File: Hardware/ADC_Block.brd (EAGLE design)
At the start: 30.5 x 44.5 mm, 28 parts, among them U1 ADS1015, U2 PCA9306

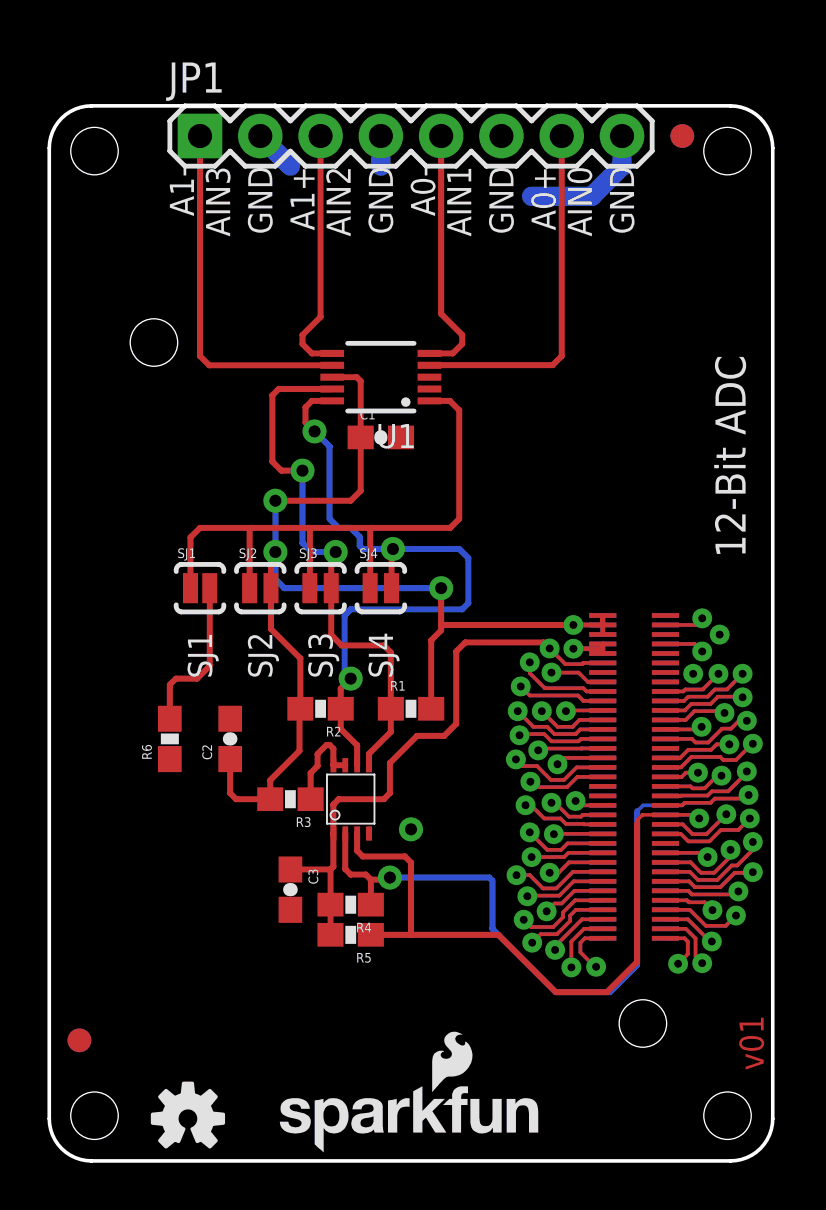
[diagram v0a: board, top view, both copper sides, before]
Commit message: Added DCIN pin Renamed boards and moved name around clenaed up copper pours clenaed up dimensions and units.
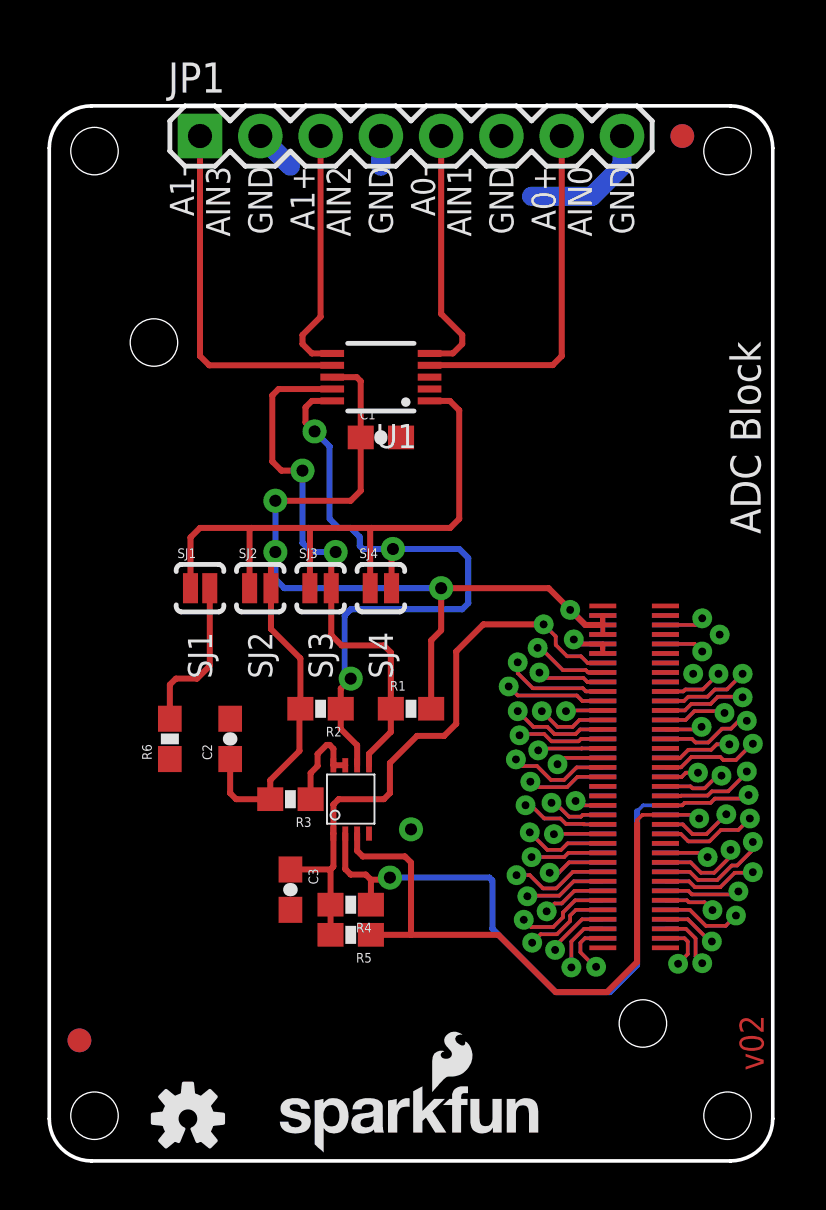
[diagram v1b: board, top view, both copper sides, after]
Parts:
- R4, R5: value 2.2k -> DNP
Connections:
- new net DCIN: U$2.14, U$3.14
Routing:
- net DCIN: track 0.00 -> 6.35 mm, vias 0 -> 1
- net 1.8V: track 26.9 -> 28.5 mm
- net VSYS: track 50.2 -> 51.2 mm
- net USB_DP: track 4.65 -> 5.67 mm
- net USB_DN: track 7.70 -> 8.72 mm
- net USB_VBUS: track 7.42 -> 8.44 mm
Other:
- board text added: "ADC Block"
- board text added: "NOTE: Units are in Inches"
- board text added: "v02"
- board text removed: "12-Bit ADC"
- board text removed: "Connectors Go Here"
- board text removed: "LED's and selector switches go here"
- board text removed: "Max Board Length"
- board text removed: "Nothing goes here... I mean it."
- board text removed: "v01"

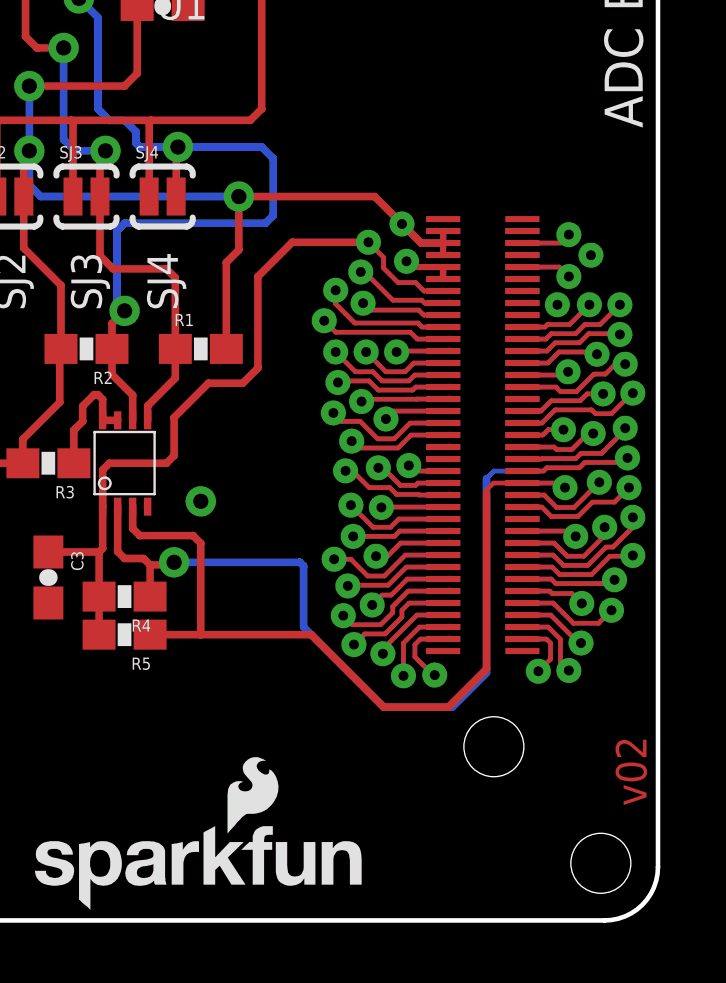
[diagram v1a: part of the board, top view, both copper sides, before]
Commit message: Chg pullups to 10k, update gnd and pwr traces, rev to 10
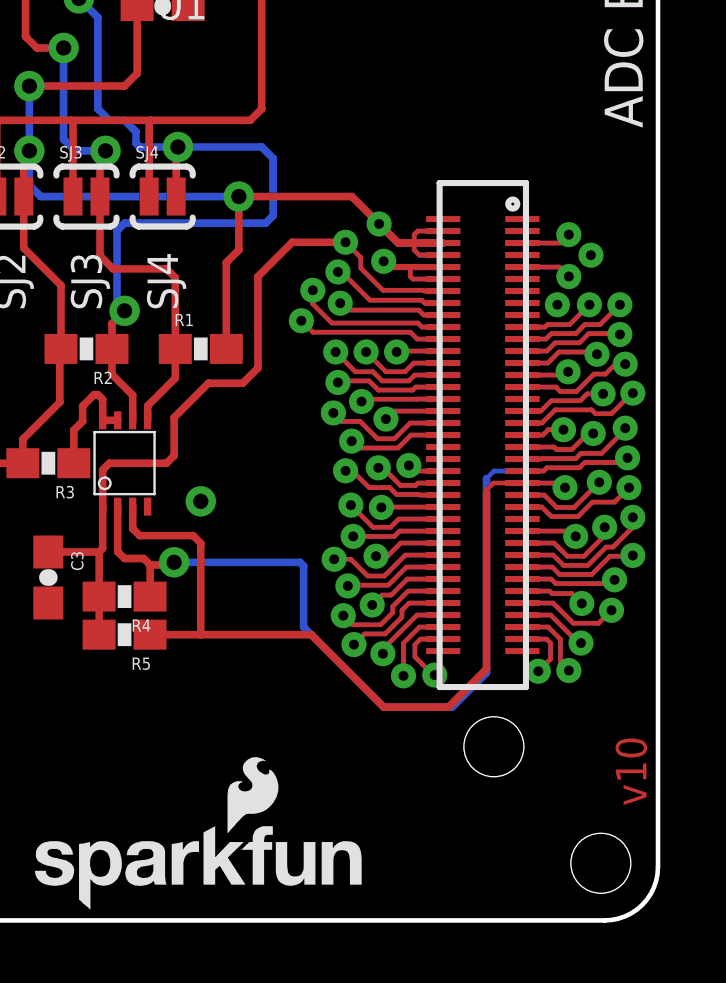
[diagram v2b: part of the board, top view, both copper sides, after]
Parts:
- R1, R2: value 2.2k -> 10K
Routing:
- net VSYS: track 51.2 -> 57.3 mm
- net 3.3V: track 3.80 -> 7.02 mm
- net USB_VBUS: track 8.44 -> 9.96 mm
- net USB_DN: track 8.72 -> 10.2 mm
- net DCIN: track 6.35 -> 7.88 mm
- net USB_DP: track 5.67 -> 7.19 mm
- net 1.8V: track 28.5 -> 29.3 mm
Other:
- board text added: "v10"
- board text removed: "v02"

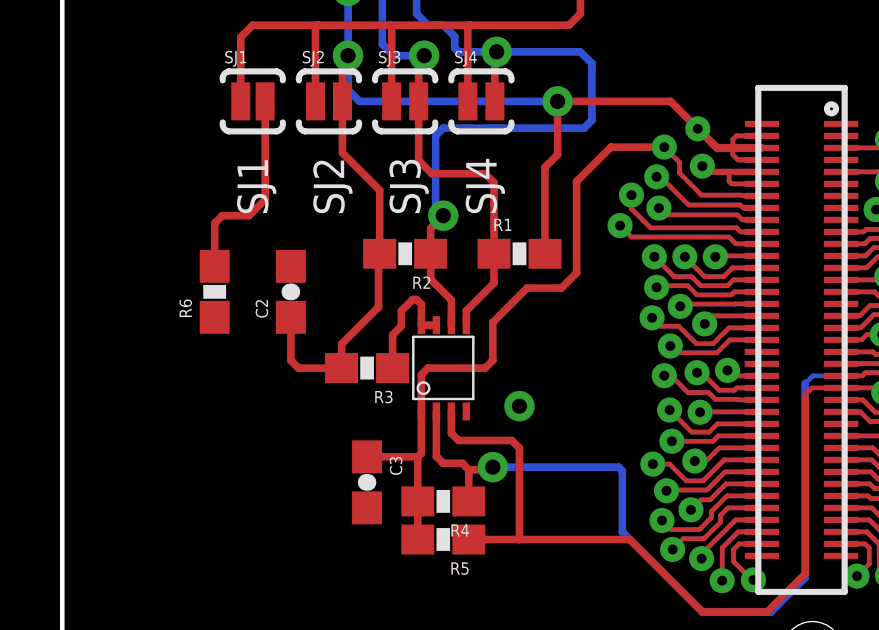
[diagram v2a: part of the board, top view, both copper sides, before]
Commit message: Rev to 10, fix pwr, gnd, txt
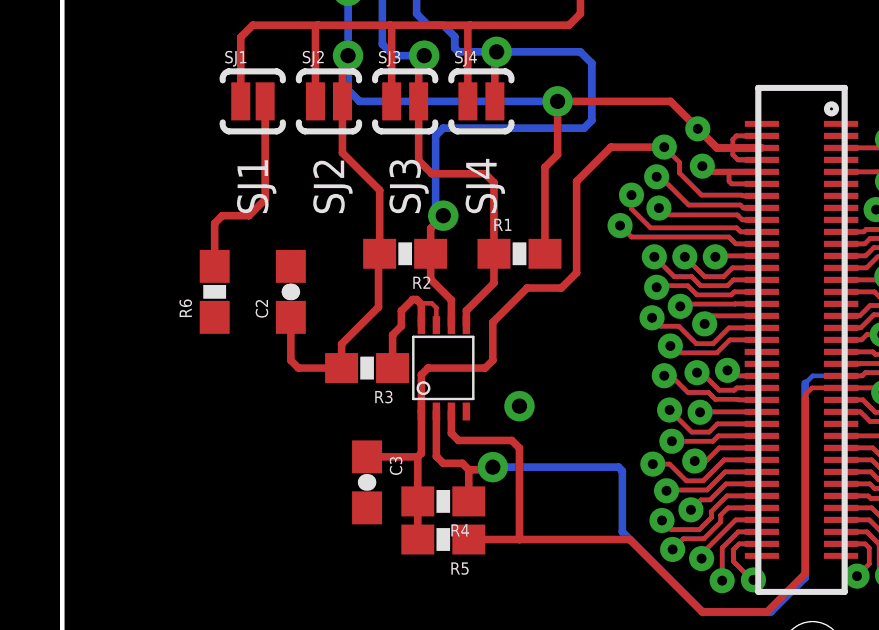
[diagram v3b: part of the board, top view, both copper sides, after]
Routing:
- net N$1: track 4.11 -> 4.77 mm
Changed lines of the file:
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@@
 <contactref element="U2" pad="8"/>
 <contactref element="U2" pad="7"/>
-<wire x1="12.47" y1="16.6708" x2="11.97" y2="16.6708" width="0.254" layer="1"/>
 <wire x1="11.97" y1="16.6708" x2="11.97" y2="17.367" width="0.254" layer="1"/>
 <wire x1="11.97" y1="17.367" x2="11.811" y2="17.526" width="0.254" layer="1"/>
@@
 <wire x1="11.303" y1="16.637" x2="11.01" y2="16.344" width="0.254" layer="1"/>
 <wire x1="11.01" y1="15.24" x2="11.01" y2="16.344" width="0.254" layer="1"/>
+<wire x1="12.47" y1="16.6708" x2="12.47" y2="17.248" width="0.1524" layer="1"/>
+<wire x1="12.47" y1="17.248" x2="12.319" y2="17.399" width="0.1524" layer="1"/>
+<wire x1="12.319" y1="17.399" x2="12.002" y2="17.399" width="0.1524" layer="1"/>
+<wire x1="12.002" y1="17.399" x2="11.97" y2="17.367" width="0.1524" layer="1"/>
 </signal>
 <signal name="HV_SCL">
